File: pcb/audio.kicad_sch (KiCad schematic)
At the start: 11 parts, among them J3 AudioJack4, U3 ES7210

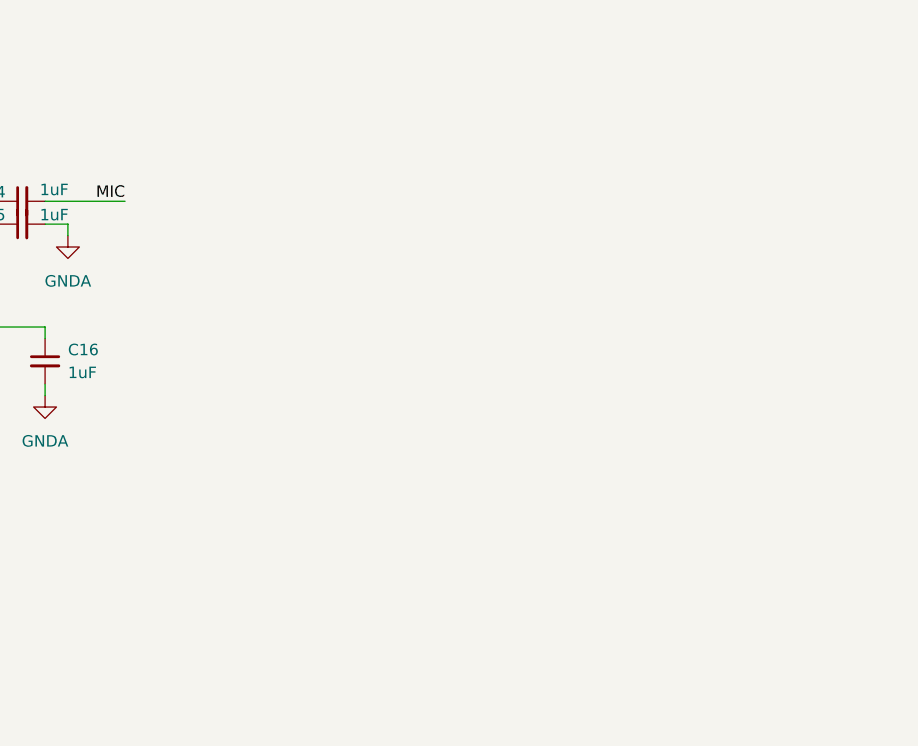
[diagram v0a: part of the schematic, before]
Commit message: pcb: Add ES8311
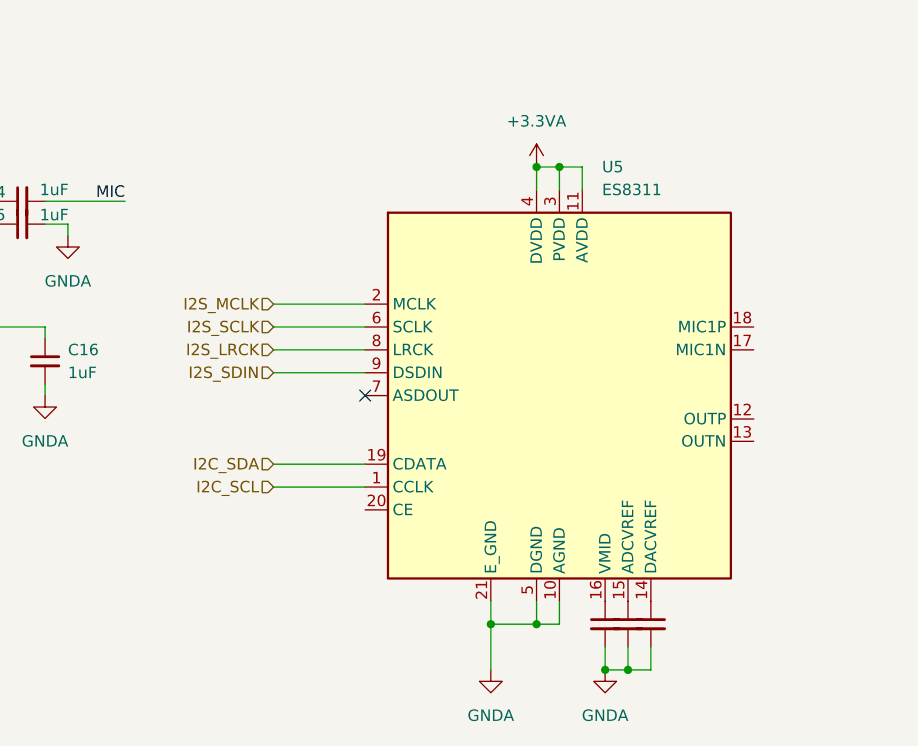
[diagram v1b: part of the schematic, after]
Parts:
- added C19, C20, C21: 1uF, symbol Device:C_Small
- added U5: ES8311, symbol live-caption-badge:ES8311
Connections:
- net +3.3VA: now also U5.11 (AVDD), U5.3 (PVDD), U5.4 (DVDD)
- net GNDA: now also C19.2, C20.2, C21.2, U5.10 (AGND), U5.21 (E_GND), U5.5 (DGND)
- net I2C_SCL: now also U5.1 (CCLK)
- net I2C_SDA: now also U5.19 (CDATA)
- net I2S_LRCK: now also U5.8 (LRCK)
- net I2S_MCLK: now also U5.2 (MCLK)
- net I2S_SCLK: now also U5.6 (SCLK)
- new net: C21.1, U5.14 (DACVREF)
- new net: C20.1, U5.15 (ADCVREF)
- new net: C19.1, U5.16 (VMID)
- new net I2S_SDIN: U5.9 (DSDIN)
- no-connect marks 9 -> 10

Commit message: caps
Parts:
- removed C19, C20, C21: 1uF, symbol Device:C_Small
- removed U5: ES8311, symbol live-caption-badge:ES8311
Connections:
- no-connect marks 10 -> 9
